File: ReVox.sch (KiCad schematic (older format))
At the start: 43 parts, among them CN1 EXPANSION_PORT, CN2 AUDIO_OUT, CN3 AUDIO_OUT, CN4 CN_RAW_DAC, U1 GAL20V8, U2 74LS273, U3 LM386

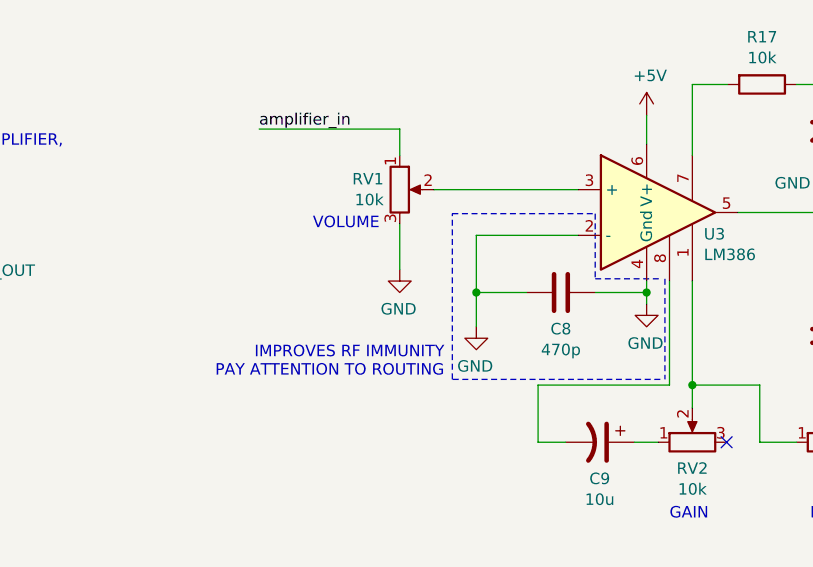
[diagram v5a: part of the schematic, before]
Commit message: Improve RF immunity
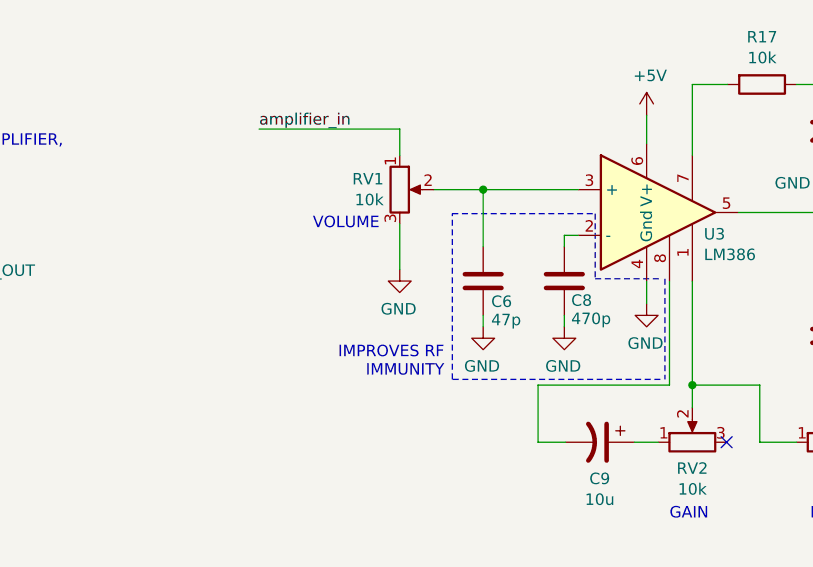
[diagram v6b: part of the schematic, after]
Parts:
- added C6: 47p, Capacitor_THT:C_Disc_D7.0mm_W2.5mm_P5.00mm, symbol Device:C
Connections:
- net GND: now also C6.1; no longer C8.2, U3.2 (-)
- net at RV1.2, U3.3 (+): now also C6.2
- new net: C8.2, U3.2 (-)
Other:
- note added: "IMPROVES RF\nIMMUNITY"
- note removed: "IMPROVES RF IMMUNITY\nPAY ATTENTION TO ROUTING"
- moved on the sheet: C8
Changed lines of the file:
@@
 	1    0    0    -1
 $EndComp
-Wire Wire Line
-	11755 6655 11755 6705
 $Comp
 L power:GND #PWR022
@@
 	1    0    0    -1
 $EndComp
-$Comp
-L Device:C C8
-U 1 1 64BADB70
-P 11380 6705
-F 0 "C8" V 11220 6705 50  0000 C CNN
-F 1 "470p" V 11129 6705 50  0000 C CNN
-F 2 "Capacitor_THT:C_Disc_D7.0mm_W2.5mm_P5.00mm" H 11418 6555 50  0001 C CNN
-F 3 "~" H 11380 6705 50  0001 C CNN
-F 4 "810-FG28C0G1H471JNT6" H 11380 6705 50  0001 C CNN "MouserPN"
-	1    11380 6705
-	0    -1   -1   0
-$EndComp
-Wire Wire Line
-	11455 6455 11010 6455
+Wire Wire Line
+	11455 6455 11395 6455
 $Comp
 L power:GND #PWR019
@@
 L power:GND #PWR020
 U 1 1 6524803C
-P 11010 6855
-F 0 "#PWR020" H 11010 6605 50  0001 C CNN
-F 1 "GND" H 11015 6682 50  0000 C CNN
-F 2 "" H 11010 6855 50  0001 C CNN
-F 3 "" H 11010 6855 50  0001 C CNN
-	1    11010 6855
+P 11395 6855
+F 0 "#PWR020" H 11395 6605 50  0001 C CNN
+F 1 "GND" H 11400 6682 50  0000 C CNN
+F 2 "" H 11395 6855 50  0001 C CNN
+F 3 "" H 11395 6855 50  0001 C CNN
+	1    11395 6855
 	-1   0    0    -1
 $EndComp
@@
 	2570 10395 2800 10395
 Wire Wire Line
-	10825 6255 11455 6255
+	10825 6255 11040 6255
 Wire Wire Line
 	10675 6405 10675 6605
@@
 $EndComp
 Wire Wire Line
-	11010 6455 11010 6705
-Wire Wire Line
-	11230 6705 11010 6705
-Connection ~ 11010 6705
-Wire Wire Line
-	11010 6705 11010 6855
-Wire Wire Line
-	11530 6705 11755 6705
-Connection ~ 11755 6705
-Wire Wire Line
-	11755 6705 11755 6755
+	11395 6455 11395 6505
 Wire Notes Line
 	10905 6360 11530 6360
@@
 	10905 7085 10905 6360
 Text Notes 10870 7080 2    50   ~ 0
-IMPROVES RF IMMUNITY\nPAY ATTENTION TO ROUTING
+IMPROVES RF\nIMMUNITY
 Text Label 11465 1685 2    50   ~ 0
 r_~w
@@
 Wire Wire Line
 	6750 6800 6750 6970
+Wire Wire Line
+	11755 6655 11755 6755
+Wire Wire Line
+	11395 6805 11395 6855
+$Comp
+L Device:C C8
+U 1 1 64BADB70
+P 11395 6655
+F 0 "C8" H 11365 6740 50  0000 R CNN
+F 1 "470p" H 11365 6820 50  0000 R CNN
+F 2 "Capacitor_THT:C_Disc_D7.0mm_W2.5mm_P5.00mm" H 11433 6505 50  0001 C CNN
+F 3 "~" H 11395 6655 50  0001 C CNN
+F 4 "810-FG28C0G1H471JNT6" H 11395 6655 50  0001 C CNN "MouserPN"
+	1    11395 6655
+	-1   0    0    1
+$EndComp
+$Comp
+L power:GND #PWR013
+U 1 1 650A8FD1
+P 11040 6855
+F 0 "#PWR013" H 11040 6605 50  0001 C CNN
+F 1 "GND" H 11045 6682 50  0000 C CNN
+F 2 "" H 11040 6855 50  0001 C CNN
+F 3 "" H 11040 6855 50  0001 C CNN
+	1    11040 6855
+	-1   0    0    -1
+$EndComp
+Wire Wire Line
+	11040 6805 11040 6855
+$Comp
+L Device:C C6
+U 1 1 650A9546
+P 11040 6655
+F 0 "C6" H 11005 6745 50  0000 R CNN
+F 1 "47p" H 11005 6825 50  0000 R CNN
+F 2 "Capacitor_THT:C_Disc_D7.0mm_W2.5mm_P5.00mm" H 11078 6505 50  0001 C CNN
+F 3 "~" H 11040 6655 50  0001 C CNN
+F 4 "810-FG28C0G1H471JNT6" H 11040 6655 50  0001 C CNN "MouserPN"
+	1    11040 6655
+	-1   0    0    1
+$EndComp
+Wire Wire Line
+	11040 6255 11040 6505
 Wire Bus Line
 	11565 1885 11565 3425
@@
 Wire Bus Line
 	9365 1480 9365 3425
+Connection ~ 11040 6255
+Wire Wire Line
+	11040 6255 11455 6255
 $EndSCHEMATC

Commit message: Add P/Ns
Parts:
- C10: Notes (none) -> Optional
- C11: MouserPN (none) -> 810-FA28X7R1H33300; Notes (none) -> Skip if Bass control is not desired
- C12: MouserPN (none) -> 810-FG28X7R1H473KNT6
- C13: MouserPN (none) -> 710-860020574012
- C5: MouserPN (none) -> 810-FG28X7R1H103KNT6; Notes (none) -> Optional, filters DAC output
- C6: MouserPN 810-FG28C0G1H471JNT6 -> 810-FG28C0G1H470JNT6; Notes (none) -> Optional, improves RF immunity
- C9, RV2: Notes (none) -> Skip if Gain control is not desired
- R17: Notes (none) -> Optional, can probably use 11K to reduce different parts co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
- R18: MouserPN (none) -> 603-MFR-25FTE52-10R
- RV3: Notes (none) -> Skip if Bass control is not desired
- U1: MouserPN (none) -> 556-AF22LV10CQZ-30PU; Notes (none) -> Or buy an old GAL22V10 from AliExpress
- U2: MouserPN (none) -> 595-SN74HCT273N
- U3: MouserPN (none) -> 926-LM386N-1/NOPB
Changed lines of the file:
@@
 F 2 "Package_DIP:DIP-24_W7.62mm_Socket_LongPads" H 10465 2285 50  0001 C CNN
 F 3 "" H 10465 2285 50  0001 C CNN
+F 4 "556-AF22LV10CQZ-30PU" H 10465 2285 50  0001 C CNN "MouserPN"
+F 5 "Or buy an old GAL22V10 from AliExpress" H 10465 2285 50  0001 C CNN "Notes"
 	1    10465 2285
 	1    0    0    -1
@@
 F 2 "Capacitor_THT:C_Disc_D7.0mm_W2.5mm_P5.00mm" H 6343 6595 50  0001 C CNN
 F 3 "~" H 6305 6745 50  0001 C CNN
+F 4 "810-FG28X7R1H103KNT6" H 6305 6745 50  0001 C CNN "MouserPN"
+F 5 "Optional, filters DAC output" H 6305 6745 50  0001 C CNN "Notes"
 	1    6305 6745
 	-1   0    0    1
@@
 F 2 "Package_DIP:DIP-8_W7.62mm_Socket_LongPads" H 11855 6455 50  0001 C CNN
 F 3 "" H 11955 6555 50  0000 C CNN
+F 4 "926-LM386N-1/NOPB" H 11755 6355 50  0001 C CNN "MouserPN"
 	1    11755 6355
 	1    0    0    -1
@@
 F 3 "~" H 12260 5795 50  0001 C CNN
 F 4 "603-MFR-25FTF52-10K" H 12260 5795 50  0001 C CNN "MouserPN"
+F 5 "Optional, can probably use 11K to reduce different parts count" H 12260 5795 50  0001 C CNN "Notes"
 	1    12260 5795
 	0    1    1    0
@@
 F 3 "~" H 12560 5990 50  0001 C CNN
 F 4 "710-860010472002" H 12560 5990 50  0001 C CNN "MouserPN"
+F 5 "Optional" H 12560 5990 50  0001 C CNN "Notes"
 	1    12560 5990
 	1    0    0    -1
@@
 F 2 "Resistor_THT:R_Axial_DIN0207_L6.3mm_D2.5mm_P10.16mm_Horizontal" V 13075 6895 50  0001 C CNN
 F 3 "~" H 13145 6895 50  0001 C CNN
+F 4 "603-MFR-25FTE52-10R" H 13145 6895 50  0001 C CNN "MouserPN"
 	1    13145 6895
 	-1   0    0    1
@@
 F 2 "Capacitor_THT:CP_Radial_D8.0mm_P3.50mm" H 13610 6355 50  0001 C CNN
 F 3 "~" H 13610 6355 50  0001 C CNN
+F 4 "710-860020574012" H 13610 6355 50  0001 C CNN "MouserPN"
 	1    13610 6355
 	0    -1   -1   0
@@
 F 2 "Capacitor_THT:C_Disc_D7.0mm_W2.5mm_P5.00mm" H 13183 6405 50  0001 C CNN
 F 3 "~" H 13145 6555 50  0001 C CNN
+F 4 "810-FG28X7R1H473KNT6" H 13145 6555 50  0001 C CNN "MouserPN"
 	1    13145 6555
 	1    0    0    -1
@@
 F 3 "~" H 11955 7360 50  0001 C CNN
 F 4 "652-3306P-1-103" H 11955 7360 50  0001 C CNN "MouserPN"
+F 5 "Skip if Gain control is not desired" H 11955 7360 50  0001 C CNN "Notes"
 	1    11955 7360
 	0    -1   -1   0
@@
 F 3 "~" H 11550 7360 50  0001 C CNN
 F 4 "710-860020573008" H 11550 7360 50  0001 C CNN "MouserPN"
+F 5 "Skip if Gain control is not desired" H 11550 7360 50  0001 C CNN "Notes"
 	1    11550 7360
 	0    1    1    0
@@
 F 3 "~" H 12560 7360 50  0001 C CNN
 F 4 "652-3306P-1-103" H 12560 7360 50  0001 C CNN "MouserPN"
+F 5 "Skip if Bass control is not desired" H 12560 7360 50  0001 C CNN "Notes"
 	1    12560 7360
 	0    -1   -1   0
@@
 F 2 "Capacitor_THT:C_Disc_D7.0mm_W2.5mm_P5.00mm" H 12598 6745 50  0001 C CNN
 F 3 "~" H 12560 6895 50  0001 C CNN
+F 4 "Skip if Bass control is not desired" H 12560 6895 50  0001 C CNN "Notes"
+F 5 "810-FA28X7R1H33300" H 12560 6895 50  0001 C CNN "MouserPN"
 	1    12560 6895
 	1    0    0    -1
@@
 F 2 "Package_DIP:DIP-20_W7.62mm_Socket_LongPads" H 14050 2250 50  0001 C CNN
 F 3 "http://www.ti.com/lit/gpn/sn74LS273" H 14050 2250 50  0001 C CNN
+F 4 "595-SN74HCT273N" H 14050 2250 50  0001 C CNN "MouserPN"
 	1    14050 2250
 	1    0    0    -1
@@
 F 2 "Capacitor_THT:C_Disc_D7.0mm_W2.5mm_P5.00mm" H 11078 6505 50  0001 C CNN
 F 3 "~" H 11040 6655 50  0001 C CNN
-F 4 "810-FG28C0G1H471JNT6" H 11040 6655 50  0001 C CNN "MouserPN"
+F 4 "810-FG28C0G1H470JNT6" H 11040 6655 50  0001 C CNN "MouserPN"
+F 5 "Optional, improves RF immunity" H 11040 6655 50  0001 C CNN "Notes"
 	1    11040 6655
 	-1   0    0    1
@@
 Wire Wire Line
 	11040 6255 11040 6505
+Connection ~ 11040 6255
 Wire Bus Line
 	11565 1885 11565 3425
@@
 Wire Bus Line
 	9365 1480 9365 3425
-Connection ~ 11040 6255
 Wire Wire Line
 	11040 6255 11455 6255

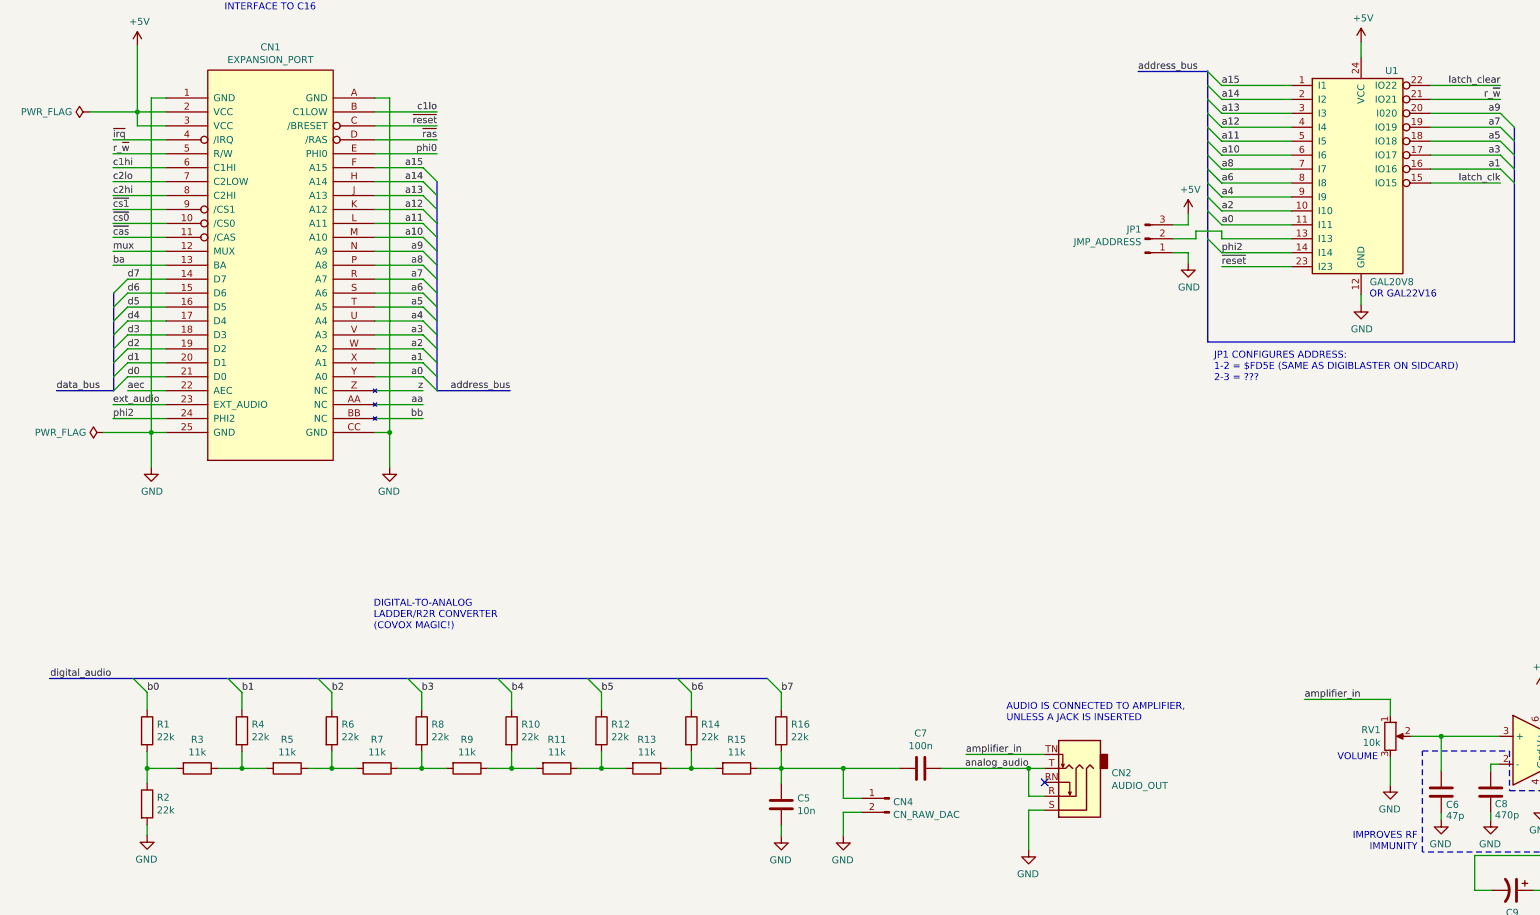
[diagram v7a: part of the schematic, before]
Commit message: Add volume wiper series resistor
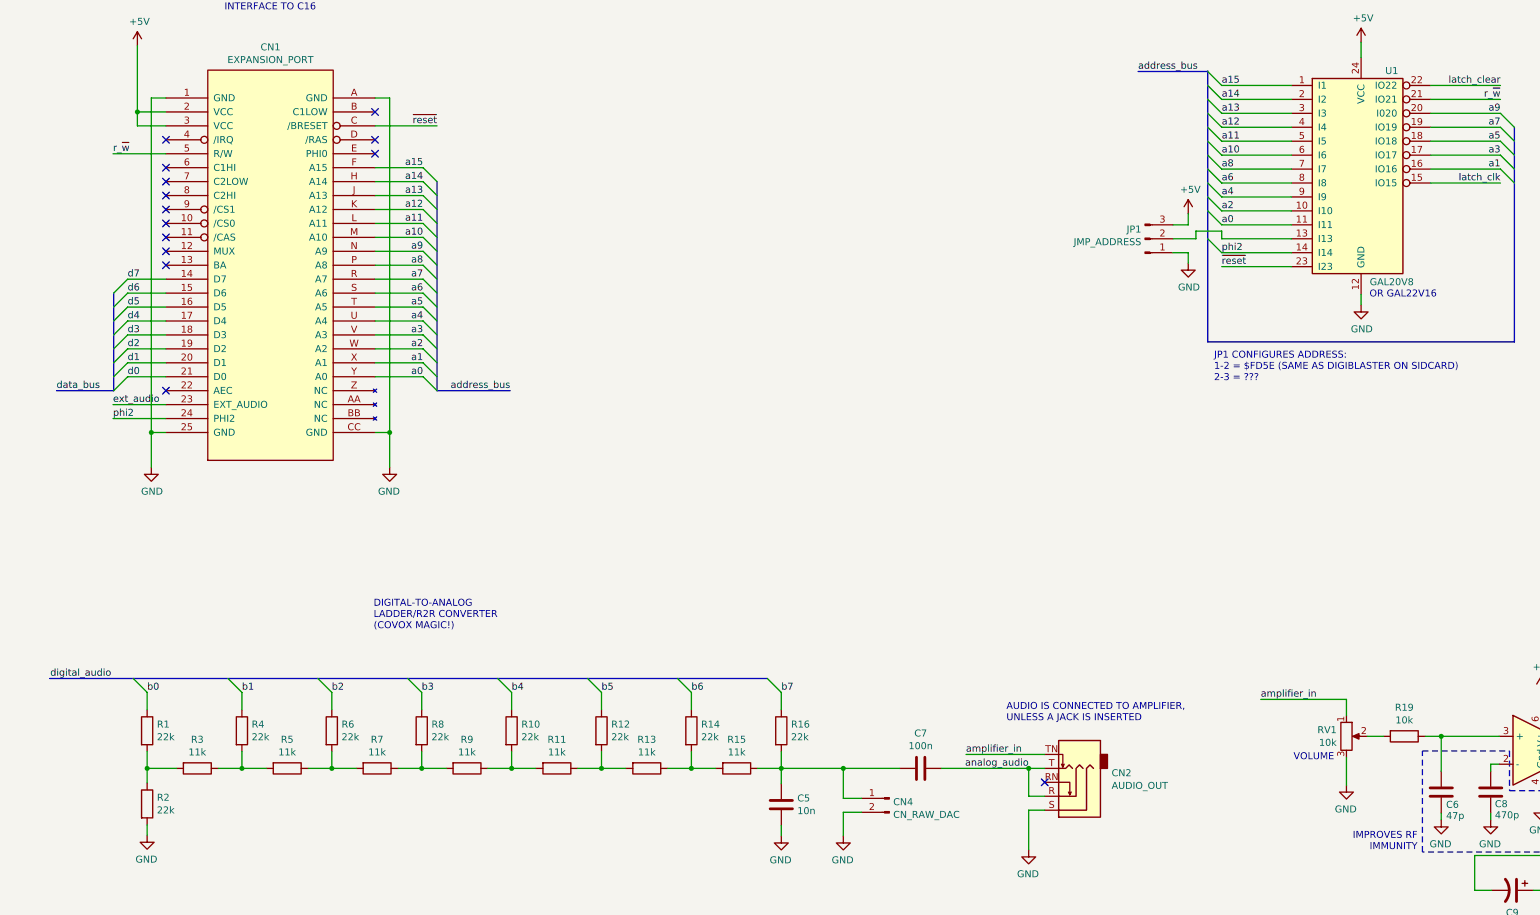
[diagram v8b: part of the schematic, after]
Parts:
- added R19: 10k, Resistor_THT:R_Axial_DIN0207_L6.3mm_D2.5mm_P10.16mm_Horizontal, symbol Device:R
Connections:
- net at C6.2, U3.3 (+): now also R19.1; no longer RV1.2
- net aa: no longer names the net of CN1.AA (NC)
- net aec: no longer names the net of CN1.22 (AEC)
- net ba: no longer names the net of CN1.13 (BA)
- net bb: no longer names the net of CN1.BB (NC)
- net c1hi: no longer names the net of CN1.6 (C1HI)
- net c1lo: no longer names the net of CN1.B (C1LOW)
- net c2hi: no longer names the net of CN1.8 (C2HI)
- net c2lo: no longer names the net of CN1.7 (C2LOW)
- net mux: no longer names the net of CN1.12 (MUX)
- net phi0: no longer names the net of CN1.E (PHI0)
- net z: no longer names the net of CN1.Z (NC)
- net ~cas: no longer names the net of CN1.11 (/CAS)
- net ~cs0: no longer names the net of CN1.10 (/CS0)
- net ~cs1: no longer names the net of CN1.9 (/CS1)
- net ~irq: no longer names the net of CN1.4 (/IRQ)
- net ~ras: no longer names the net of CN1.D (/RAS)
- new net: R19.2, RV1.2
- no-connect marks 4 -> 17
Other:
- moved on the sheet: RV1
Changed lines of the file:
@@
 Sheet 1 1
 Title "ReVox"
-Date "2023-08-20"
+Date "2023-08-22"
 Rev "1git"
 Comp "SukkoPera"
@@
 Text Notes 2310 1055 0    50   ~ 0
 INTERFACE TO C16
-$Comp
-L power:PWR_FLAG #FLG01
-U 1 1 63505677
-P 1345 1775
-F 0 "#FLG01" H 1345 1850 50  0001 C CNN
-F 1 "PWR_FLAG" V 1345 1902 50  0000 L CNN
-F 2 "" H 1345 1775 50  0001 C CNN
-F 3 "~" H 1345 1775 50  0001 C CNN
-	1    1345 1775
-	0    -1   -1   0
-$EndComp
-Wire Wire Line
-	1345 1775 1685 1775
-$Comp
-L power:PWR_FLAG #FLG02
-U 1 1 6351F7AE
-P 1445 4075
-F 0 "#FLG02" H 1445 4150 50  0001 C CNN
-F 1 "PWR_FLAG" V 1445 4202 50  0000 L CNN
-F 2 "" H 1445 4075 50  0001 C CNN
-F 3 "~" H 1445 4075 50  0001 C CNN
-	1    1445 4075
-	0    -1   -1   0
-$EndComp
-Wire Wire Line
-	1445 4075 1785 4075
 Text Notes 1435 9020 0    50   ~ 0
 DECOUPLING & POWER
@@
 L power:GND #PWR019
 U 1 1 64BCB190
-P 10675 6605
-F 0 "#PWR019" H 10675 6355 50  0001 C CNN
-F 1 "GND" H 10680 6432 50  0000 C CNN
-F 2 "" H 10675 6605 50  0001 C CNN
-F 3 "" H 10675 6605 50  0001 C CNN
-	1    10675 6605
-	-1   0    0    -1
-$EndComp
-Wire Wire Line
-	10675 6105 10675 5990
-Wire Wire Line
-	10675 5990 10060 5990
-Text Label 10060 5990 0    50   ~ 0
+P 10360 6605
+F 0 "#PWR019" H 10360 6355 50  0001 C CNN
+F 1 "GND" H 10365 6432 50  0000 C CNN
+F 2 "" H 10360 6605 50  0001 C CNN
+F 3 "" H 10360 6605 50  0001 C CNN
+	1    10360 6605
+	-1   0    0    -1
+$EndComp
+Wire Wire Line
+	10360 6105 10360 5990
+Wire Wire Line
+	10360 5990 9745 5990
+Text Label 9745 5990 0    50   ~ 0
 amplifier_in
 Wire Wire Line
@@
 	11280 7110 11280 7360
 NoConn ~ 12105 7360
-Text Notes 10295 6435 0    50   ~ 0
+Text Notes 9980 6435 0    50   ~ 0
 VOLUME
 Text Notes 11855 7705 0    50   ~ 0
@@
 	2570 10395 2800 10395
 Wire Wire Line
-	10825 6255 11040 6255
-Wire Wire Line
-	10675 6405 10675 6605
+	10510 6255 10625 6255
+Wire Wire Line
+	10360 6405 10360 6605
 Wire Wire Line
 	12560 6355 13145 6355
@@
 $EndComp
 Wire Wire Line
-	1890 1975 1510 1975
-Text Label 1510 1975 0    50   ~ 0
-~irq
-Wire Wire Line
-	1890 2175 1510 2175
-Wire Wire Line
-	1890 2275 1510 2275
-Wire Wire Line
-	1890 2375 1510 2375
-Wire Wire Line
-	1890 2475 1510 2475
-Wire Wire Line
-	1890 2575 1510 2575
-Wire Wire Line
-	1890 2675 1510 2675
-Wire Wire Line
-	1890 2775 1510 2775
-Wire Wire Line
-	1890 2875 1510 2875
-Text Label 1510 2175 0    50   ~ 0
-c1hi
-Text Label 1510 2275 0    50   ~ 0
-c2lo
-Text Label 1510 2375 0    50   ~ 0
-c2hi
-Text Label 1510 2475 0    50   ~ 0
-~cs1
-Text Label 1510 2575 0    50   ~ 0
-~cs0
-Text Label 1510 2675 0    50   ~ 0
-~cas
-Text Label 1510 2775 0    50   ~ 0
-mux
-Text Label 1510 2875 0    50   ~ 0
-ba
-Wire Wire Line
-	1890 3775 1615 3775
-Text Label 1615 3775 0    50   ~ 0
-aec
-Wire Wire Line
-	3390 1775 3835 1775
-Wire Wire Line
-	3390 1975 3835 1975
-Wire Wire Line
-	3390 2075 3835 2075
-Text Label 3835 1775 2    50   ~ 0
-c1lo
-Text Label 3835 1975 2    50   ~ 0
-~ras
-Text Label 3835 2075 2    50   ~ 0
-phi0
-Wire Wire Line
-	3390 3775 3735 3775
-Wire Wire Line
-	3390 3875 3735 3875
-Wire Wire Line
-	3390 3975 3735 3975
-Text Label 3735 3775 2    50   ~ 0
-z
-Text Label 3735 3875 2    50   ~ 0
-aa
-Text Label 3735 3975 2    50   ~ 0
-bb
-Wire Wire Line
 	1080 9800 1080 9925
 Wire Wire Line
@@
 L Device:R_POT RV1
 U 1 1 64B82196
-P 10675 6255
-F 0 "RV1" H 10605 6301 50  0000 R CNN
-F 1 "10k" H 10605 6210 50  0000 R CNN
-F 2 "ReVox:Pot_Bourns_3306P" H 10675 6255 50  0001 C CNN
-F 3 "~" H 10675 6255 50  0001 C CNN
-F 4 "652-3306P-1-103" H 10675 6255 50  0001 C CNN "MouserPN"
-	1    10675 6255
+P 10360 6255
+F 0 "RV1" H 10290 6301 50  0000 R CNN
+F 1 "10k" H 10290 6210 50  0000 R CNN
+F 2 "ReVox:Pot_Bourns_3306P" H 10360 6255 50  0001 C CNN
+F 3 "~" H 10360 6255 50  0001 C CNN
+F 4 "652-3306P-1-103" H 10360 6255 50  0001 C CNN "MouserPN"
+	1    10360 6255
 	1    0    0    -1
 $EndComp
@@
 	11040 6255 11040 6505
 Connection ~ 11040 6255
+$Comp
+L Device:R R19
+U 1 1 65103B76
+P 10775 6255
+F 0 "R19" V 10568 6255 50  0000 C CNN
+F 1 "10k" V 10659 6255 50  0000 C CNN
+F 2 "Resistor_THT:R_Axial_DIN0207_L6.3mm_D2.5mm_P10.16mm_Horizontal" V 10705 6255 50  0001 C CNN
+F 3 "~" H 10775 6255 50  0001 C CNN
+F 4 "603-MFR-25FTF52-10K" H 10775 6255 50  0001 C CNN "MouserPN"
+F 5 "Optional, can probably use 11K to reduce different parts count" H 10775 6255 50  0001 C CNN "Notes"
+	1    10775 6255
+	0    1    1    0
+$EndComp
+Wire Wire Line
+	10925 6255 11040 6255
+Wire Wire Line
+	11040 6255 11455 6255
+NoConn ~ 1890 3775
+NoConn ~ 1890 1975
+NoConn ~ 1890 2175
+NoConn ~ 1890 2275
+NoConn ~ 1890 2375
+NoConn ~ 1890 2475
+NoConn ~ 1890 2575
+NoConn ~ 1890 2675
+NoConn ~ 1890 2775
+NoConn ~ 1890 2875
+NoConn ~ 3390 1775
+NoConn ~ 3390 1975
+NoConn ~ 3390 2075
 Wire Bus Line
 	11565 1885 11565 3425
@@
 Wire Bus Line
 	9365 1480 9365 3425
-Wire Wire Line
-	11040 6255 11455 6255
 $EndSCHEMATC
